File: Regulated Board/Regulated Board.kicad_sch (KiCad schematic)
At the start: 144 parts, among them J1 Screw_Terminal_01x02, J10 Screw_Terminal_01x02, J11 Screw_Terminal_01x20, J12 Screw_Terminal_01x20, J13 Screw_Terminal_01x02, J14 Conn_01x01_MountingPin, J15 Conn_01x01_MountingPin, J16 Conn_01x01_MountingPin, J2 Screw_Terminal_01x02, J3 Screw_Terminal_01x20, J4 Screw_Terminal_01x02, J5 Screw_Terminal_01x02, J6 Screw_Terminal_01x02, J7 Screw_Terminal_01x20, J8 Screw_Terminal_01x20, J9 Screw_Terminal_01x20, Q1 IRLZ44N, Q3 IRLZ44N, Q4 IRLZ44N

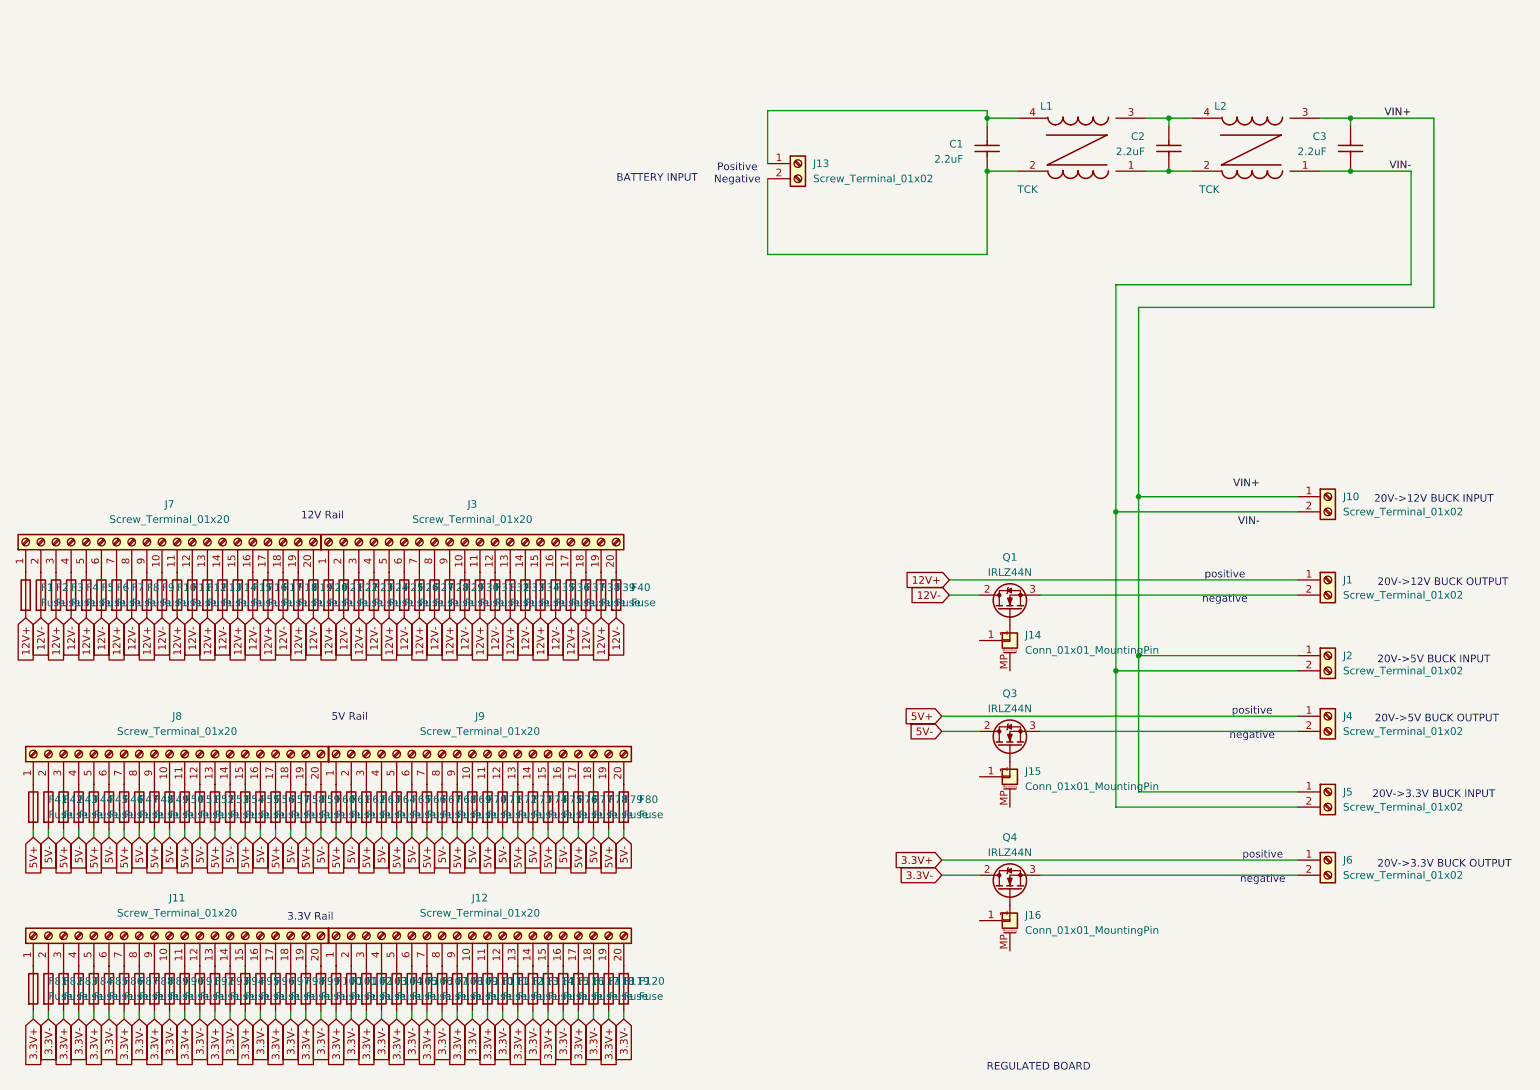
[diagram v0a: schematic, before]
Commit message: Added more fuses
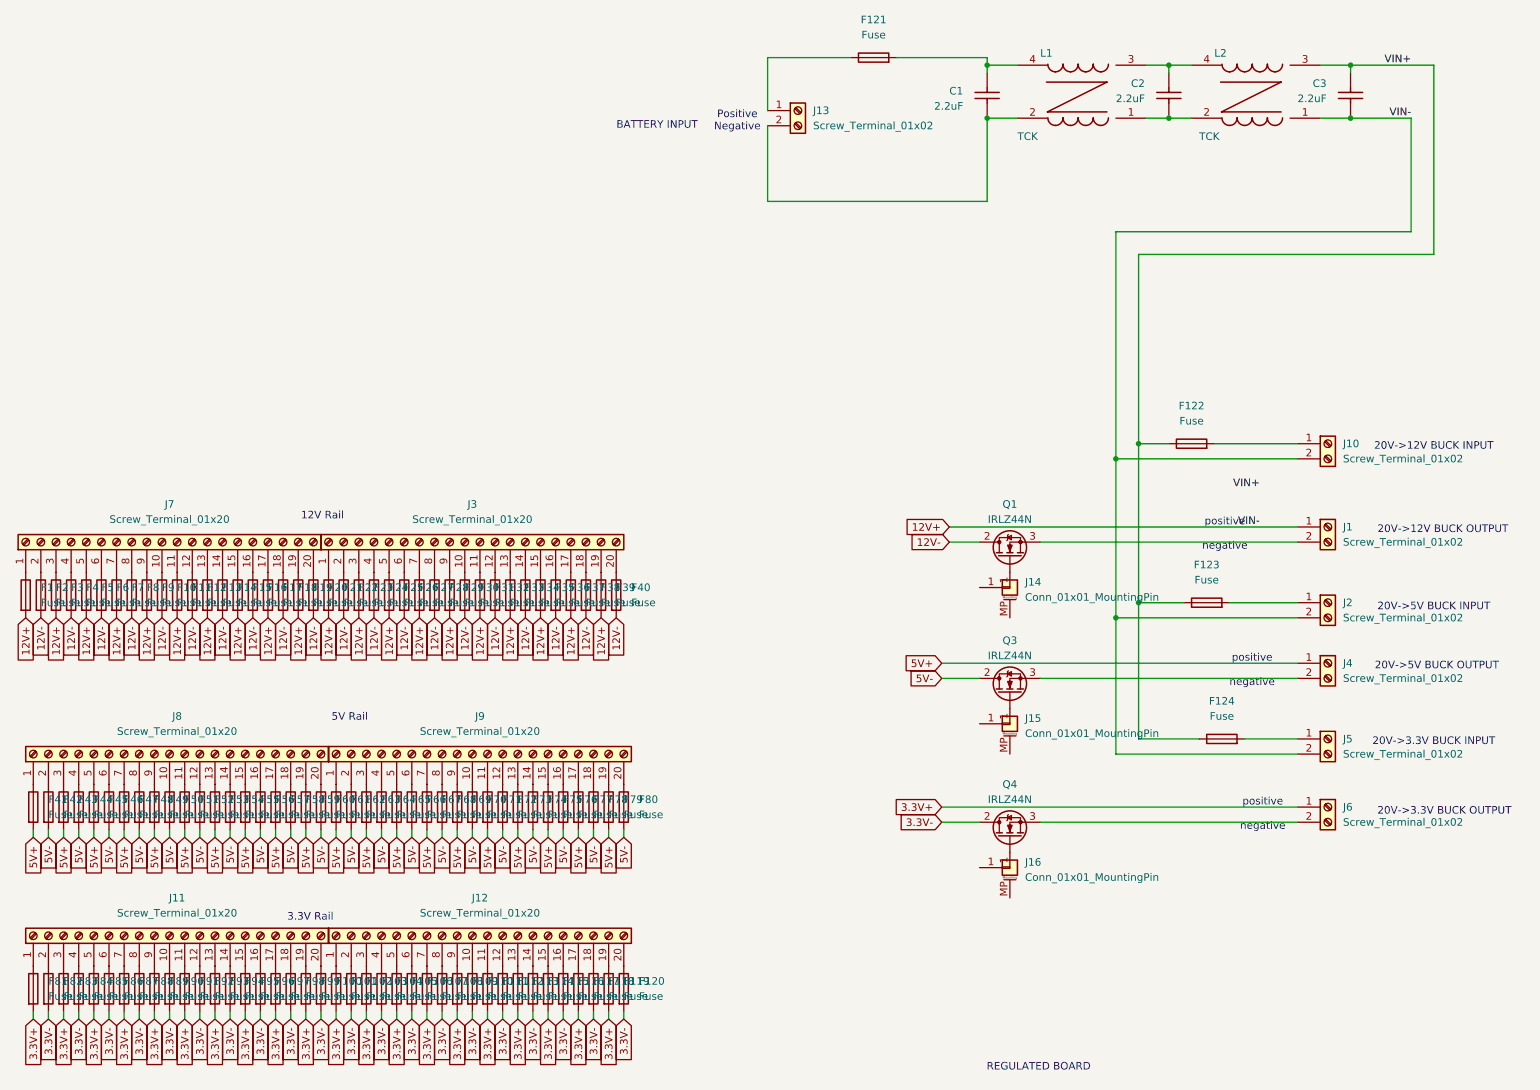
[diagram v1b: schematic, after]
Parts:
- added F121, F122, F123, F124: Fuse, symbol Device:Fuse
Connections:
- net VIN- is gone; now on net 12V+: C3.2, J10.2 (Pin_2), J2.2 (Pin_2), J5.2 (Pin_2), L2.1
- net VIN+: now also F122.1, F123.1, F124.1; no longer J10.1 (Pin_1), J2.1 (Pin_1), J5.1 (Pin_1)
- net at C1.1, L1.4 (2): now also F121.2; no longer J13.1 (Pin_1)
- new net: F123.2, J2.1 (Pin_1)
- new net: F121.1, J13.1 (Pin_1)
- new net: F122.2, J10.1 (Pin_1)
- new net: F124.2, J5.1 (Pin_1)
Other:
- moved on the sheet: C1, C2, C3, J1, J10, J13, J14, J15, J16, J2, J4, J5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

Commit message: Assigned footprints to all components
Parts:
- C1, C2, C3: footprint PDB:SMD Cap -> Capacitor_THT:CP_Radial_D5.0mm_P2.00mm
- F1, F10, F100, F101, F102, F103, F104, F105, F106, F107, F108, F109, F11, F110, F111, F112, F113, F114, F115, F116, F117, F118, F119, F12, F120, F121, F122, F123, F124, F13, F14, F15, F16, F17, F18, F19, F2, F20, F21, F22, F23, F24, F25, F26, F27, F28, F29, F3, F30, F31, F32, F33, F34, F35, F36, F37, F38, F39, F4, F40, F41, F42, F43, F44, F45, F46, F47, F48, F49, F5, F50, F51, F52, F53, F54, F55, F56, F57, F58, F59, F6, F60, F61, F62, F63, F64, F65, F66, F67, F68, F69, F7, F70, F71, F72, F73, F74, F75, F76, F77, F78, F79, F8, F80, F81, F82, F83, F84, F85, F86, F87, F88, F89, F9, F90, F91, F92, F93, F94, F95, F96, F97, F98, F99: footprint (none) -> Resistor_THT:R_Axial_Power_L20.0mm_W6.4mm_P22.40mm
- J1, J10, J13, J2, J4, J5, J6: footprint (none) -> Connector_PinHeader_2.54mm:PinHeader_1x02_P2.54mm_Vertical
- J11, J12, J3, J7, J8, J9: footprint (none) -> Connector_PinHeader_2.54mm:PinHeader_1x20_P2.54mm_Vertical
- J14, J15, J16: footprint (none) -> Connector_PinHeader_1.00mm:PinHeader_1x01_P1.00mm_Vertical
- L1, L2: footprint PDB:TCK Choke -> Library:TCK-076

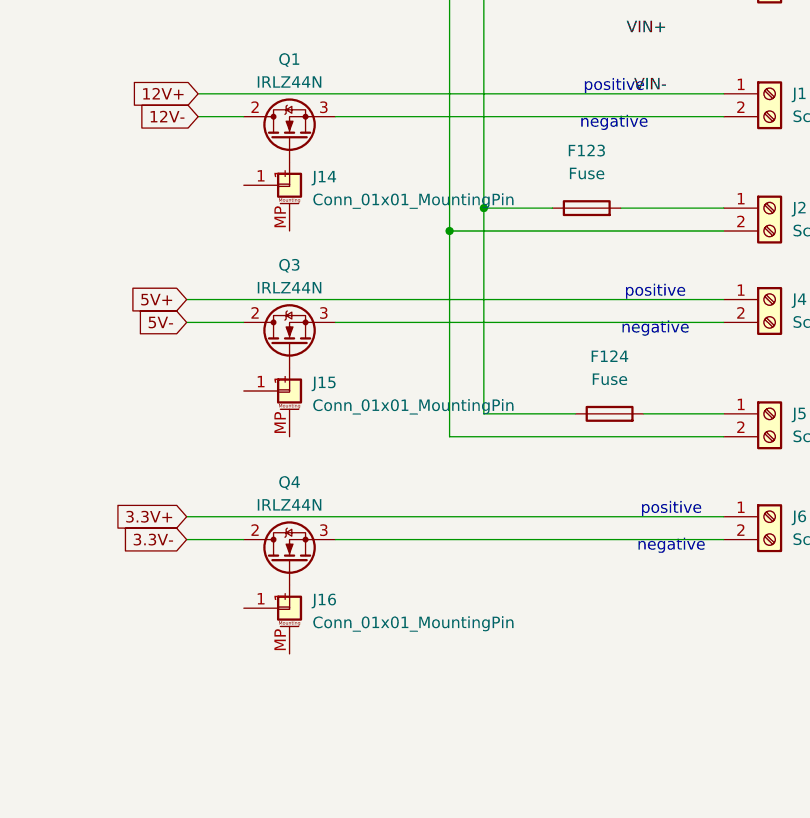
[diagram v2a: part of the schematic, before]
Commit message: Added a lot of footprints and did some PCB layout
Need to find footprints and appropriate screw terminals. Will route.
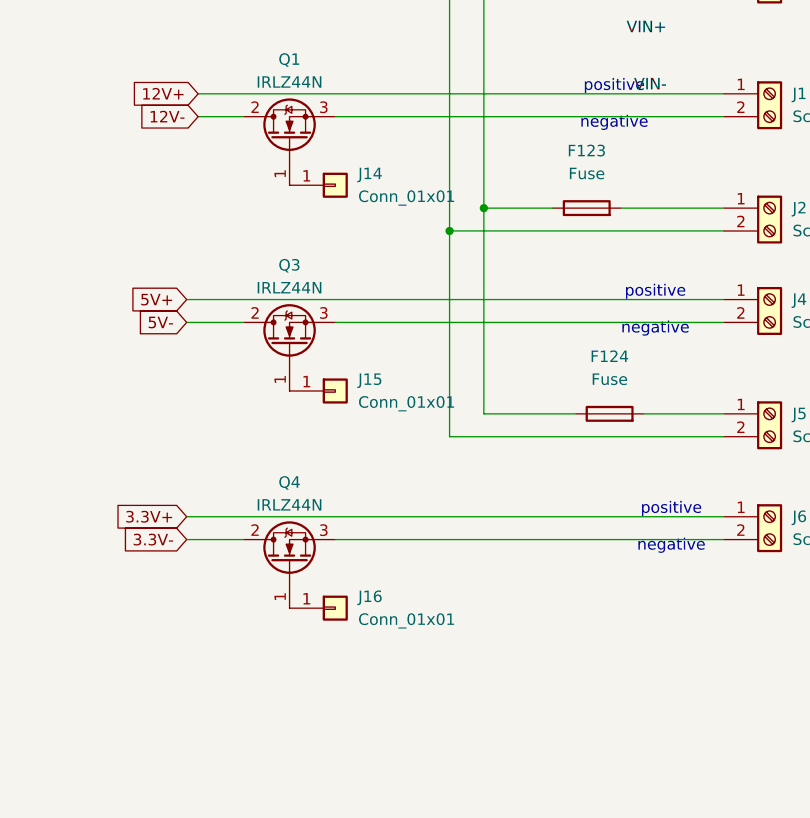
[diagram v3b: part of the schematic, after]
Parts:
- removed J14, J15, J16: Conn_01x01_MountingPin, Connector_PinHeader_1.00mm:PinHeader_1x01_P1.00mm_Vertical, symbol Connector_Generic_MountingPin:Conn_01x01_MountingPin
- added J14, J15, J16: Conn_01x01, Connector_PinHeader_2.54mm:PinHeader_1x01_P2.54mm_Vertical, symbol Connector_Generic:Conn_01x01
- F1, F10, F100, F101, F102, F103, F104, F105, F106, F107, F108, F109, F11, F110, F111, F112, F113, F114, F115, F116, F117, F118, F119, F12, F120, F121, F122, F123, F124, F13, F14, F15, F16, F17, F18, F19, F2, F20, F21, F22, F23, F24, F25, F26, F27, F28, F29, F3, F30, F31, F32, F33, F34, F35, F36, F37, F38, F39, F4, F40, F41, F42, F43, F44, F45, F46, F47, F48, F49, F5, F50, F51, F52, F53, F54, F55, F56, F57, F58, F59, F6, F60, F61, F62, F63, F64, F65, F66, F67, F68, F69, F7, F70, F71, F72, F73, F74, F75, F76, F77, F78, F79, F8, F80, F81, F82, F83, F84, F85, F86, F87, F88, F89, F9, F90, F91, F92, F93, F94, F95, F96, F97, F98, F99: footprint Resistor_THT:R_Axial_Power_L20.0mm_W6.4mm_P22.40mm -> Library:FUSE_3544-2
- J11, J12, J3, J7, J8, J9: footprint Connector_PinHeader_2.54mm:PinHeader_1x20_P2.54mm_Vertical -> (none)
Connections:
- net at Q4.1 (G): now also J16.1 (Pin_1)
- net at Q1.1 (G): now also J14.1 (Pin_1)
- net at Q3.1 (G): now also J15.1 (Pin_1)
